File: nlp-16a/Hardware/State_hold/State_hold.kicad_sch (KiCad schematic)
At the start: 15 parts, among them J1 Conn_01x08_Male, J2 Conn_01x08_Male, J3 Conn_01x08_Male, J4 Conn_01x08_Male, J5 Conn_01x08_Male, J6 Conn_01x08_Male, J7 Conn_01x08_Male, J8 Conn_01x08_Male, J9 Conn_01x02_Male

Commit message: ステート保持ラッチ再設計．おそらく問題無し
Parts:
- removed J1, J2, J3, J4, J5, J6, J7, J8: Conn_01x08_Male, Connector_PinHeader_2.54mm:PinHeader_1x08_P2.54mm_Vertical, symbol Connector:Conn_01x08_Male
- removed J9: Conn_01x02_Male, Connector_PinHeader_2.54mm:PinHeader_1x02_P2.54mm_Vertical, symbol Connector:Conn_01x02_Male
- added J1, J10, J11, J12, J2, J3, J4, J5, J6, J7, J8, J9: Conn_01x05_Female, Connector_PinSocket_2.54mm:PinSocket_1x05_P2.54mm_Vertical, symbol Connector:Conn_01x05_Female
- added J13: Conn_01x02_Male, Connector_PinHeader_2.54mm:PinHeader_1x02_P2.54mm_Vertical, symbol Connector:Conn_01x02_Male
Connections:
- net GND: now also J13.2 (Pin_2)
- net VCC: now also J13.1 (Pin_1)
- new net State_latch0/D: J1.1 (Pin_1)
- new net State_latch0/Gate: J1.2 (Pin_2), J11.2 (Pin_2), J3.2 (Pin_2), J5.2 (Pin_2), J7.2 (Pin_2), J9.2 (Pin_2)
- new net State_latch0/LED: J1.4 (Pin_4)
- new net State_latch0/Q: J1.3 (Pin_3)
- new net State_latch0/~{Q}: J1.5 (Pin_5)
- new net State_latch1/D: J2.1 (Pin_1)
- new net State_latch1/Gate: J10.2 (Pin_2), J12.2 (Pin_2), J2.2 (Pin_2), J4.2 (Pin_2), J6.2 (Pin_2), J8.2 (Pin_2)
- new net State_latch1/LED: J2.4 (Pin_4)
- new net State_latch1/Q: J2.3 (Pin_3)
- new net State_latch1/~{Q}: J2.5 (Pin_5)
- new net State_latch10/D: J11.1 (Pin_1)
- new net State_latch10/LED: J11.4 (Pin_4)
- new net State_latch10/Q: J11.3 (Pin_3)
- new net State_latch10/~{Q}: J11.5 (Pin_5)
- new net State_latch11/D: J12.1 (Pin_1)
- new net State_latch11/LED: J12.4 (Pin_4)
- new net State_latch11/Q: J12.3 (Pin_3)
- new net State_latch11/~{Q}: J12.5 (Pin_5)
- new net State_latch2/D: J3.1 (Pin_1)
- new net State_latch2/LED: J3.4 (Pin_4)
- new net State_latch2/Q: J3.3 (Pin_3)
- new net State_latch2/~{Q}: J3.5 (Pin_5)
- new net State_latch3/D: J4.1 (Pin_1)
- new net State_latch3/LED: J4.4 (Pin_4)
- new net State_latch3/Q: J4.3 (Pin_3)
- new net State_latch3/~{Q}: J4.5 (Pin_5)
- new net State_latch4/D: J5.1 (Pin_1)
- new net State_latch4/LED: J5.4 (Pin_4)
- new net State_latch4/Q: J5.3 (Pin_3)
- new net State_latch4/~{Q}: J5.5 (Pin_5)
- new net State_latch5/D: J6.1 (Pin_1)
- new net State_latch5/LED: J6.4 (Pin_4)
- new net State_latch5/Q: J6.3 (Pin_3)
- new net State_latch5/~{Q}: J6.5 (Pin_5)
- new net State_latch6/D: J7.1 (Pin_1)
- new net State_latch6/LED: J7.4 (Pin_4)
- new net State_latch6/Q: J7.3 (Pin_3)
- new net State_latch6/~{Q}: J7.5 (Pin_5)
- new net State_latch7/D: J8.1 (Pin_1)
- new net State_latch7/LED: J8.4 (Pin_4)
- new net State_latch7/Q: J8.3 (Pin_3)
- new net State_latch7/~{Q}: J8.5 (Pin_5)
- new net State_latch8/D: J9.1 (Pin_1)
- new net State_latch8/LED: J9.4 (Pin_4)
- new net State_latch8/Q: J9.3 (Pin_3)
- new net State_latch8/~{Q}: J9.5 (Pin_5)
- new net State_latch9/D: J10.1 (Pin_1)
- new net State_latch9/LED: J10.4 (Pin_4)
- new net State_latch9/Q: J10.3 (Pin_3)
- new net State_latch9/~{Q}: J10.5 (Pin_5)
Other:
- removed sheet State_hold_unit0
- removed sheet State_hold_unit1
- removed sheet State_hold_unit10
- removed sheet State_hold_unit11
- removed sheet State_hold_unit2
- removed sheet State_hold_unit3
- removed sheet State_hold_unit4
- removed sheet State_hold_unit5
- removed sheet State_hold_unit6
- removed sheet State_hold_unit7
- removed sheet State_hold_unit8
- removed sheet State_hold_unit9
- added sheet State_latch0 (State_latch.kicad_sch)
- added sheet State_latch1 (State_latch.kicad_sch)
- added sheet State_latch10 (State_latch.kicad_sch)
- added sheet State_latch11 (State_latch.kicad_sch)
- added sheet State_latch2 (State_latch.kicad_sch)
- added sheet State_latch3 (State_latch.kicad_sch)
- added sheet State_latch4 (State_latch.kicad_sch)
- added sheet State_latch5 (State_latch.kicad_sch)
- added sheet State_latch6 (State_latch.kicad_sch)
- added sheet State_latch7 (State_latch.kicad_sch)
- added sheet State_latch8 (State_latch.kicad_sch)
- added sheet State_latch9 (State_latch.kicad_sch)

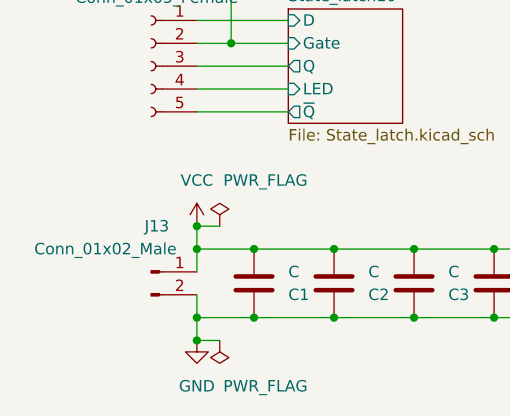
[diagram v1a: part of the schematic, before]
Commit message: 軽微な修正を加えてガーバー作成 発注
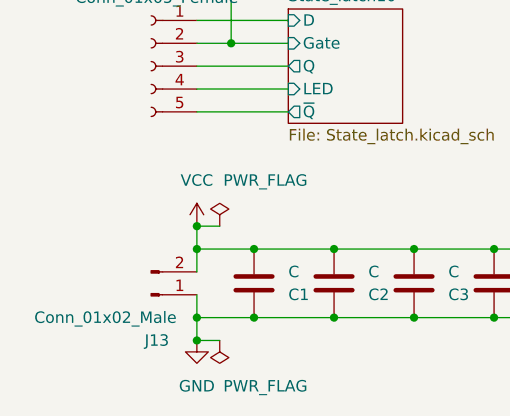
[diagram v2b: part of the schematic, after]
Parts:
- C1, C2, C3, C4, C5, C6: footprint Capacitor_THT:C_Disc_D7.5mm_W2.5mm_P5.00mm -> Capacitor_THT:C_Disc_D7.0mm_W2.5mm_P5.00mm
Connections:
- net GND: now also J13.1 (Pin_1); no longer J13.2 (Pin_2)
- net VCC: now also J13.2 (Pin_2); no longer J13.1 (Pin_1)
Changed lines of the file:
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@@
       (effects (font (size 1.27 1.27)) (justify left))
     )
-    (property "Footprint" "Capacitor_THT:C_Disc_D7.5mm_W2.5mm_P5.00mm" (id 2) (at 147.0152 156.21 0)
+    (property "Footprint" "Capacitor_THT:C_Disc_D7.0mm_W2.5mm_P5.00mm" (id 2) (at 147.0152 156.21 0)
       (effects (font (size 1.27 1.27)) hide)
     )
@@
       (effects (font (size 1.27 1.27)) (justify left))
     )
-    (property "Footprint" "Capacitor_THT:C_Disc_D7.5mm_W2.5mm_P5.00mm" (id 2) (at 138.1252 156.21 0)
+    (property "Footprint" "Capacitor_THT:C_Disc_D7.0mm_W2.5mm_P5.00mm" (id 2) (at 138.1252 156.21 0)
       (effects (font (size 1.27 1.27)) hide)
     )
@@
       (effects (font (size 1.27 1.27)) (justify left))
     )
-    (property "Footprint" "Capacitor_THT:C_Disc_D7.5mm_W2.5mm_P5.00mm" (id 2) (at 111.4552 156.21 0)
+    (property "Footprint" "Capacitor_THT:C_Disc_D7.0mm_W2.5mm_P5.00mm" (id 2) (at 111.4552 156.21 0)
       (effects (font (size 1.27 1.27)) hide)
     )
@@
       (effects (font (size 1.27 1.27)) (justify left))
     )
-    (property "Footprint" "Capacitor_THT:C_Disc_D7.5mm_W2.5mm_P5.00mm" (id 2) (at 120.3452 156.21 0)
+    (property "Footprint" "Capacitor_THT:C_Disc_D7.0mm_W2.5mm_P5.00mm" (id 2) (at 120.3452 156.21 0)
       (effects (font (size 1.27 1.27)) hide)
     )
@@
     (pin "5")
   )
-  (symbol (lib_id "Connector:Conn_01x02_Male") (at 99.06 158.75 0) (unit 1)
+  (symbol (lib_id "Connector:Conn_01x02_Male") (at 99.06 161.29 0) (mirror x) (unit 1)
     (in_bom yes) (on_board yes)
-    (property "Reference" "J13" (id 0) (at 99.695 153.67 0))
-    (property "Value" "Conn_01x02_Male" (id 1) (at 93.98 156.21 0))
-    (property "Footprint" "Connector_PinHeader_2.54mm:PinHeader_1x02_P2.54mm_Vertical" (id 2) (at 99.06 158.75 0)
-      (effects (font (size 1.27 1.27)) hide)
-    )
-    (property "Datasheet" "~" (id 3) (at 99.06 158.75 0)
+    (property "Reference" "J13" (id 0) (at 99.695 166.37 0))
+    (property "Value" "Conn_01x02_Male" (id 1) (at 93.98 163.83 0))
+    (property "Footprint" "Connector_PinHeader_2.54mm:PinHeader_1x02_P2.54mm_Vertical" (id 2) (at 99.06 161.29 0)
+      (effects (font (size 1.27 1.27)) hide)
+    )
+    (property "Datasheet" "~" (id 3) (at 99.06 161.29 0)
       (effects (font (size 1.27 1.27)) hide)
     )
@@
       (effects (font (size 1.27 1.27)) (justify left))
     )
-    (property "Footprint" "Capacitor_THT:C_Disc_D7.5mm_W2.5mm_P5.00mm" (id 2) (at 129.2352 156.21 0)
+    (property "Footprint" "Capacitor_THT:C_Disc_D7.0mm_W2.5mm_P5.00mm" (id 2) (at 129.2352 156.21 0)
       (effects (font (size 1.27 1.27)) hide)
     )
@@
       (effects (font (size 1.27 1.27)) (justify left))
     )
-    (property "Footprint" "Capacitor_THT:C_Disc_D7.5mm_W2.5mm_P5.00mm" (id 2) (at 155.9052 156.21 0)
+    (property "Footprint" "Capacitor_THT:C_Disc_D7.0mm_W2.5mm_P5.00mm" (id 2) (at 155.9052 156.21 0)
       (effects (font (size 1.27 1.27)) hide)
     )
@@
     )
     (path "/8cf4dc3b-4fba-4e6b-a195-148a3a547d54"
-      (reference "C1") (unit 1) (value "C") (footprint "Capacitor_THT:C_Disc_D7.5mm_W2.5mm_P5.00mm")
+      (reference "C1") (unit 1) (value "C") (footprint "Capacitor_THT:C_Disc_D7.0mm_W2.5mm_P5.00mm")
     )
     (path "/8e417b8b-72ae-4a9f-91fc-5c54a826081d"
-      (reference "C2") (unit 1) (value "C") (footprint "Capacitor_THT:C_Disc_D7.5mm_W2.5mm_P5.00mm")
+      (reference "C2") (unit 1) (value "C") (footprint "Capacitor_THT:C_Disc_D7.0mm_W2.5mm_P5.00mm")
     )
     (path "/a0063a91-28b2-4185-940b-921e50f59b28"
-      (reference "C3") (unit 1) (value "C") (footprint "Capacitor_THT:C_Disc_D7.5mm_W2.5mm_P5.00mm")
+      (reference "C3") (unit 1) (value "C") (footprint "Capacitor_THT:C_Disc_D7.0mm_W2.5mm_P5.00mm")
     )
     (path "/5e675b96-263c-408a-b975-fb47a89ec192"
-      (reference "C4") (unit 1) (value "C") (footprint "Capacitor_THT:C_Disc_D7.5mm_W2.5mm_P5.00mm")
+      (reference "C4") (unit 1) (value "C") (footprint "Capacitor_THT:C_Disc_D7.0mm_W2.5mm_P5.00mm")
     )
     (path "/14213465-a33f-494d-9dd9-3ef23498c325"
-      (reference "C5") (unit 1) (value "C") (footprint "Capacitor_THT:C_Disc_D7.5mm_W2.5mm_P5.00mm")
+      (reference "C5") (unit 1) (value "C") (footprint "Capacitor_THT:C_Disc_D7.0mm_W2.5mm_P5.00mm")
     )
     (path "/a9bc7529-dc37-428d-9f95-2ba160f88258"
-      (reference "C6") (unit 1) (value "C") (footprint "Capacitor_THT:C_Disc_D7.5mm_W2.5mm_P5.00mm")
+      (reference "C6") (unit 1) (value "C") (footprint "Capacitor_THT:C_Disc_D7.0mm_W2.5mm_P5.00mm")
     )
     (path "/4a26f424-9966-48a9-af5e-838cc9d3e851/2a1a6d2f-253c-4998-8c56-3aed1a77a933"
